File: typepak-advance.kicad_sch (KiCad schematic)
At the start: 25 parts, among them J2 Conn_01x04, J3 Conn_01x02, J5 Conn_01x32_Pin, J6 Conn_01x10, Q1 AO3407, Q2 AO3407, U1 E73-2G4M08S1C, U2 AP2112K-3.3, U3 TP4054, X1 32768kHz

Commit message: Initial Commit.
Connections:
- net P0.17: now also J5.17 (Pin_17); no longer J5.23 (Pin_23)
- net P0.22: now also J5.18 (Pin_18); no longer J5.25 (Pin_25)
- net P0.28: now also J5.23 (Pin_23); no longer J5.16 (Pin_16)
- net P1.02: now also J5.16 (Pin_16); no longer J5.17 (Pin_17)
- net P1.04: now also J5.25 (Pin_25); no longer J5.18 (Pin_18)
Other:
- note added: "LowF+A"
- moved on the sheet: R1
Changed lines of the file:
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@@
 		)
 	)
-	(text "LowF"
+	(text "LowF+A"
 		(exclude_from_sim no)
-		(at 43.18 93.472 90)
+		(at 43.18 92.202 90)
 		(effects
 			(font
@@
 		)
 	)
-	(text "LowF"
+	(text "LowF+A"
 		(exclude_from_sim no)
-		(at 48.26 93.472 90)
+		(at 48.26 92.202 90)
 		(effects
 			(font
@@
 		)
 	)
-	(text "LowF"
+	(text "LowF+A"
 		(exclude_from_sim no)
-		(at 58.42 93.472 90)
+		(at 76.2 92.202 90)
 		(effects
 			(font
@@
 	(text "LowF"
 		(exclude_from_sim no)
-		(at 60.96 93.472 90)
+		(at 58.42 93.472 90)
 		(effects
 			(font
@@
 	(text "USB Power"
 		(exclude_from_sim no)
-		(at 27.686 115.57 90)
+		(at 20.066 115.57 90)
 		(effects
 			(font
@@
 	(text "HighF"
 		(exclude_from_sim no)
-		(at 76.2 93.218 90)
+		(at 60.96 93.218 90)
 		(effects
 			(font
@@
 	(text "HighF"
 		(exclude_from_sim no)
-		(at 81.28 93.218 90)
+		(at 63.5 93.218 90)
 		(effects
 			(font
@@
 	(text "GND"
 		(exclude_from_sim no)
-		(at 20.32 112.522 90)
+		(at 27.94 112.522 90)
 		(effects
 			(font
@@
 		)
 	)
-	(text "LowF"
+	(text "LowF+A"
 		(exclude_from_sim no)
-		(at 40.64 93.472 90)
+		(at 40.64 92.202 90)
 		(effects
 			(font
@@
 		)
 	)
-	(text "LowF"
+	(text "LowF+A"
 		(exclude_from_sim no)
-		(at 63.5 93.472 90)
+		(at 81.28 92.202 90)
 		(effects
 			(font
@@
 		)
 	)
-	(text "LowF"
+	(text "LowF+A"
 		(exclude_from_sim no)
-		(at 38.1 93.472 90)
+		(at 38.1 92.202 90)
 		(effects
 			(font
@@
 	)
 	(junction
-		(at 49.53 148.59)
+		(at 27.94 148.59)
 		(diameter 0)
 		(color 0 0 0 0)
 	)
 	(junction
-		(at 43.815 148.59)
+		(at 49.53 148.59)
 		(diameter 0)
 		(color 0 0 0 0)
 	)
 	(junction
-		(at 133.35 83.82)
+		(at 27.94 139.7)
 		(diameter 0)
 		(color 0 0 0 0)
 	)
 	(junction
-		(at 133.35 91.44)
+		(at 43.815 148.59)
 		(diameter 0)
 		(color 0 0 0 0)
 	)
 	(junction
-		(at 133.35 101.6)
+		(at 133.35 83.82)
 		(diameter 0)
 		(color 0 0 0 0)
 	)
 	(junction
-		(at 214.63 142.24)
+		(at 133.35 91.44)
 		(diameter 0)
 		(color 0 0 0 0)
 	)
 	(junction
-		(at 149.86 88.9)
+		(at 133.35 101.6)
 		(diameter 0)
 		(color 0 0 0 0)
 	)
 	(junction
-		(at 27.305 139.7)
+		(at 214.63 142.24)
 		(diameter 0)
 		(color 0 0 0 0)
 	)
 	(junction
-		(at 96.52 137.795)
+		(at 149.86 88.9)
 		(diameter 0)
 		(color 0 0 0 0)
 	)
 	(junction
-		(at 27.305 148.59)
+		(at 96.52 137.795)
 		(diameter 0)
 		(color 0 0 0 0)
@@
 	(wire
 		(pts
-			(xy 27.305 161.29) (xy 27.305 162.56)
+			(xy 27.94 157.48) (xy 27.94 158.75)
 		)
 		(stroke
@@
 	(wire
 		(pts
+			(xy 27.94 139.7) (xy 36.195 139.7)
+		)
+		(stroke
+			(width 0)
+			(type default)
+		)
+	)
+	(wire
+		(pts
 			(xy 49.53 151.13) (xy 49.53 148.59)
 		)
@@
 	(wire
 		(pts
-			(xy 27.305 139.7) (xy 24.765 139.7)
+			(xy 24.765 139.7) (xy 27.94 139.7)
 		)
 		(stroke
@@
 	(wire
 		(pts
-			(xy 142.24 147.955) (xy 144.78 147.955)
+			(xy 27.94 148.59) (xy 27.94 149.86)
 		)
 		(stroke
@@
 	(wire
 		(pts
-			(xy 33.02 52.07) (xy 41.91 52.07)
+			(xy 142.24 147.955) (xy 144.78 147.955)
 		)
 		(stroke
@@
 	(wire
 		(pts
-			(xy 27.305 139.7) (xy 36.195 139.7)
+			(xy 33.02 52.07) (xy 41.91 52.07)
 		)
 		(stroke
@@
 	(wire
 		(pts
-			(xy 251.46 25.4) (xy 261.62 25.4)
+			(xy 27.94 139.7) (xy 27.94 148.59)
 		)
 		(stroke
@@
 	(wire
 		(pts
-			(xy 33.02 57.15) (xy 41.91 57.15)
+			(xy 251.46 25.4) (xy 261.62 25.4)
 		)
 		(stroke
@@
 	(wire
 		(pts
-			(xy 33.02 67.31) (xy 41.91 67.31)
+			(xy 33.02 57.15) (xy 41.91 57.15)
 		)
 		(stroke
@@
 	(wire
 		(pts
-			(xy 149.86 88.9) (xy 162.56 88.9)
+			(xy 33.02 67.31) (xy 41.91 67.31)
 		)
 		(stroke
@@
 	(wire
 		(pts
-			(xy 53.975 151.13) (xy 49.53 151.13)
+			(xy 149.86 88.9) (xy 162.56 88.9)
 		)
 		(stroke
@@
 	(wire
 		(pts
-			(xy 41.91 69.85) (xy 33.02 69.85)
+			(xy 53.975 151.13) (xy 49.53 151.13)
 		)
 		(stroke
@@
 	(wire
 		(pts
-			(xy 83.82 64.77) (xy 76.2 64.77)
+			(xy 41.91 69.85) (xy 33.02 69.85)
 		)
 		(stroke
@@
 	(wire
 		(pts
-			(xy 41.91 77.47) (xy 32.385 77.47)
+			(xy 83.82 64.77) (xy 76.2 64.77)
 		)
 		(stroke
@@
 	(wire
 		(pts
-			(xy 27.305 148.59) (xy 27.305 153.67)
+			(xy 41.91 77.47) (xy 32.385 77.47)
 		)
 		(stroke
@@
 	(wire
 		(pts
-			(xy 27.305 139.7) (xy 27.305 148.59)
-		)
-		(stroke
-			(width 0)
-			(type default)
-		)
-	)
-	(wire
-		(pts
-			(xy 27.305 148.59) (xy 31.75 148.59)
+			(xy 27.94 148.59) (xy 31.75 148.59)
 		)
 		(stroke
@@
 	(global_label "P1.04"
 		(shape input)
-		(at 63.5 104.14 90)
+		(at 81.28 104.14 90)
 		(fields_autoplaced yes)
 		(effects
@@
 		)
 		(property "Intersheetrefs" "${INTERSHEET_REFS}"
-			(at 63.5 95.6515 90)
+			(at 81.28 95.6515 90)
 			(effects
 				(font
@@
 	(global_label "P0.28"
 		(shape input)
-		(at 58.42 104.14 90)
+		(at 76.2 104.14 90)
 		(fields_autoplaced yes)
 		(effects
@@
 		)
 		(property "Intersheetrefs" "${INTERSHEET_REFS}"
-			(at 58.42 95.6515 90)
+			(at 76.2 95.6515 90)
 			(effects
 				(font
@@
 	(global_label "P0.22"
 		(shape input)
-		(at 81.28 104.14 90)
+		(at 63.5 104.14 90)
 		(fields_autoplaced yes)
 		(effects
@@
 		)
 		(property "Intersheetrefs" "${INTERSHEET_REFS}"
-			(at 81.28 95.6515 90)
+			(at 63.5 95.6515 90)
 			(effects
 				(font
@@
 	(global_label "P1.02"
 		(shape input)
-		(at 60.96 104.14 90)
+		(at 58.42 104.14 90)
 		(fields_autoplaced yes)
 		(effects
@@
 		)
 		(property "Intersheetrefs" "${INTERSHEET_REFS}"
-			(at 60.96 95.6515 90)
+			(at 58.42 95.6515 90)
 			(effects
 				(font
@@
 	(global_label "P0.17"
 		(shape input)
-		(at 76.2 104.14 90)
+		(at 60.96 104.14 90)
 		(fields_autoplaced yes)
 		(effects
@@
 		)
 		(property "Intersheetrefs" "${INTERSHEET_REFS}"
-			(at 76.2 95.6515 90)
+			(at 60.96 95.6515 90)
 			(effects
 				(font
@@
 	(symbol
 		(lib_id "nrfmicro-rescue:R")
-		(at 27.305 157.48 0)
+		(at 27.94 153.67 0)
 		(unit 1)
 		(exclude_from_sim no)
@@
 		(dnp no)
 		(property "Reference" "R1"
-			(at 29.083 156.3116 0)
+			(at 29.718 152.5016 0)
 			(effects
 				(font
@@
 		)
 		(property "Value" "100K"
-			(at 29.083 158.623 0)
+			(at 29.718 154.813 0)
 			(effects
 				(font
@@
 		)
 		(property "Footprint" "Resistor_SMD:R_0805_2012Metric_Pad1.20x1.40mm_HandSolder"
-			(at 25.527 157.48 90)
+			(at 26.162 153.67 90)
 			(effects
 				(font
@@
 		)
 		(property "Datasheet" ""
-			(at 27.305 157.48 0)
+			(at 27.94 153.67 0)
 			(effects
 				(font
@@
 		)
 		(property "Description" ""
-			(at 27.305 157.48 0)
+			(at 27.94 153.67 0)
 			(effects
 				(font
@@
 	(symbol
 		(lib_id "nrfmicro-rescue:GND")
-		(at 27.305 162.56 0)
+		(at 27.94 158.75 0)
 		(unit 1)
 		(exclude_from_sim no)
@@
 		(dnp no)
 		(property "Reference" "#PWR017"
-			(at 27.305 168.91 0)
+			(at 27.94 165.1 0)
 			(effects
 				(font
@@
 		)
 		(property "Value" "GND"
-			(at 27.305 166.37 0)
+			(at 27.94 162.56 0)
 			(effects
 				(font
@@
 		)
 		(property "Footprint" ""
-			(at 27.305 162.56 0)
+			(at 27.94 158.75 0)
 			(effects
 				(font
@@
 		)
 		(property "Datasheet" ""
-			(at 27.305 162.56 0)
+			(at 27.94 158.75 0)
 			(effects
 				(font
@@
 		)
 		(property "Description" ""
-			(at 27.305 162.56 0)
+			(at 27.94 158.75 0)
 			(effects
 				(font

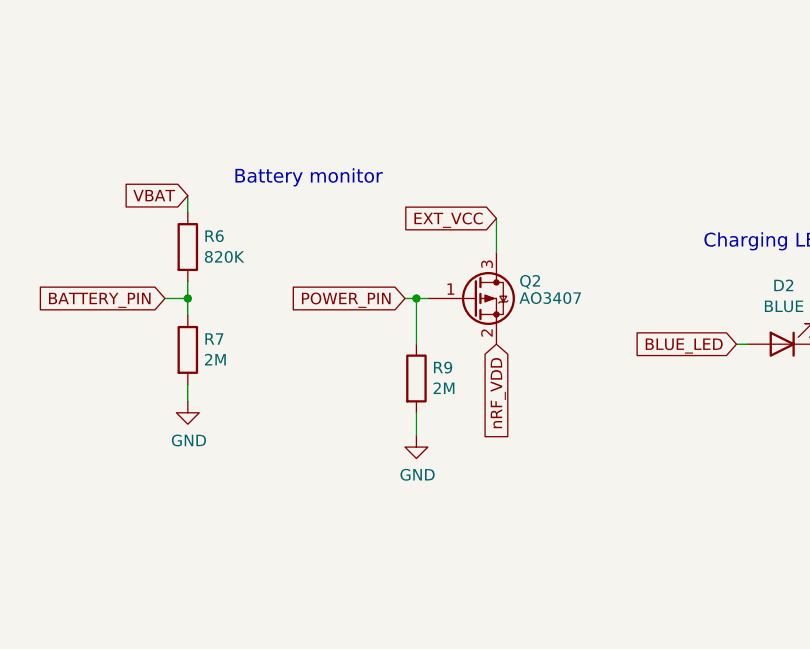
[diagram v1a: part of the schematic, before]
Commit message: Updated to hand-solder footprints.
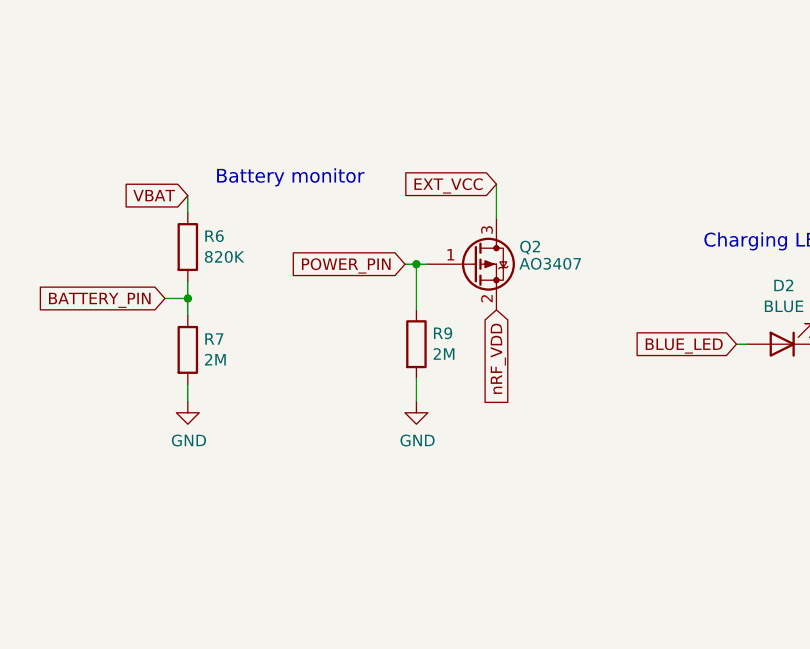
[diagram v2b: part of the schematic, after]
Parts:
- Q1, Q2: footprint Package_TO_SOT_SMD:SOT-23 -> Package_TO_SOT_SMD:SOT-23_Handsoldering
- U2, U3: footprint Package_TO_SOT_SMD:SOT-23-5 -> Package_TO_SOT_SMD:SOT-23-5_HandSoldering
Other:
- moved on the sheet: Q2, R9
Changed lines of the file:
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@@
 	(text "Battery monitor"
 		(exclude_from_sim no)
-		(at 194.31 129.794 0)
+		(at 192.278 129.794 0)
 		(effects
 			(font
@@
 	)
 	(junction
-		(at 214.63 142.24)
+		(at 214.63 138.43)
 		(diameter 0)
 		(color 0 0 0 0)
@@
 	(wire
 		(pts
-			(xy 223.52 133.35) (xy 223.52 137.16)
+			(xy 223.52 129.54) (xy 223.52 133.35)
 		)
 		(stroke
@@
 	(wire
 		(pts
-			(xy 213.36 142.24) (xy 214.63 142.24)
+			(xy 213.36 138.43) (xy 214.63 138.43)
 		)
 		(stroke
@@
 	(wire
 		(pts
-			(xy 214.63 154.94) (xy 214.63 157.48)
+			(xy 214.63 151.13) (xy 214.63 153.67)
 		)
 		(stroke
@@
 	(wire
 		(pts
-			(xy 214.63 142.24) (xy 214.63 147.32)
+			(xy 214.63 138.43) (xy 214.63 143.51)
 		)
 		(stroke
@@
 	(wire
 		(pts
-			(xy 214.63 142.24) (xy 215.9 142.24)
+			(xy 214.63 138.43) (xy 215.9 138.43)
 		)
 		(stroke
@@
 	(global_label "EXT_VCC"
 		(shape input)
-		(at 223.52 133.35 180)
+		(at 223.52 129.54 180)
 		(fields_autoplaced yes)
 		(effects
@@
 		)
 		(property "Intersheetrefs" "${INTERSHEET_REFS}"
-			(at 212.6125 133.35 0)
+			(at 212.6125 129.54 0)
 			(effects
 				(font
@@
 	(global_label "POWER_PIN"
 		(shape input)
-		(at 213.36 142.24 180)
+		(at 213.36 138.43 180)
 		(fields_autoplaced yes)
 		(effects
@@
 		)
 		(property "Intersheetrefs" "${INTERSHEET_REFS}"
-			(at 199.731 142.24 0)
+			(at 199.731 138.43 0)
 			(effects
 				(font
@@
 	(global_label "nRF_VDD"
 		(shape input)
-		(at 223.52 147.32 270)
+		(at 223.52 143.51 270)
 		(fields_autoplaced yes)
 		(effects
@@
 		)
 		(property "Intersheetrefs" "${INTERSHEET_REFS}"
-			(at 223.52 158.409 90)
+			(at 223.52 154.599 90)
 			(effects
 				(font
@@
 			)
 		)
-		(property "Footprint" "Package_TO_SOT_SMD:SOT-23"
+		(property "Footprint" "Package_TO_SOT_SMD:SOT-23_Handsoldering"
 			(at 46.355 141.605 0)
 			(effects
@@
 	(symbol
 		(lib_id "nrfmicro-rescue:BSS83P")
-		(at 220.98 142.24 0)
+		(at 220.98 138.43 0)
 		(unit 1)
 		(exclude_from_sim no)
@@
 		(dnp no)
 		(property "Reference" "Q2"
-			(at 226.06 140.335 0)
+			(at 226.06 136.525 0)
 			(effects
 				(font
@@
 		)
 		(property "Value" "AO3407"
-			(at 226.06 142.24 0)
+			(at 226.06 138.43 0)
 			(effects
 				(font
@@
 			)
 		)
-		(property "Footprint" "Package_TO_SOT_SMD:SOT-23"
-			(at 226.06 144.145 0)
+		(property "Footprint" "Package_TO_SOT_SMD:SOT-23_Handsoldering"
+			(at 226.06 140.335 0)
 			(effects
 				(font
@@
 		)
 		(property "Datasheet" ""
-			(at 220.98 142.24 0)
+			(at 220.98 138.43 0)
 			(effects
 				(font
@@
 		)
 		(property "Description" ""
-			(at 220.98 142.24 0)
+			(at 220.98 138.43 0)
 			(effects
 				(font
@@
 	(symbol
 		(lib_id "Device:R")
-		(at 214.63 151.13 0)
+		(at 214.63 147.32 0)
 		(unit 1)
 		(exclude_from_sim no)
@@
 		(dnp no)
 		(property "Reference" "R9"
-			(at 216.408 149.9616 0)
+			(at 216.408 146.1516 0)
 			(effects
 				(font
@@
 		)
 		(property "Value" "2M"
-			(at 216.408 152.273 0)
+			(at 216.408 148.463 0)
 			(effects
 				(font
@@
 		)
 		(property "Footprint" "Resistor_SMD:R_0805_2012Metric_Pad1.20x1.40mm_HandSolder"
-			(at 212.852 151.13 90)
+			(at 212.852 147.32 90)
 			(effects
 				(font
@@
 		)
 		(property "Datasheet" "~"
-			(at 214.63 151.13 0)
+			(at 214.63 147.32 0)
 			(effects
 				(font
@@
 		)
 		(property "Description" ""
-			(at 214.63 151.13 0)
+			(at 214.63 147.32 0)
 			(effects
 				(font
@@
 			)
 		)
-		(property "Footprint" "Package_TO_SOT_SMD:SOT-23-5"
+		(property "Footprint" "Package_TO_SOT_SMD:SOT-23-5_HandSoldering"
 			(at 123.19 151.765 0)
 			(effects
@@
 			)
 		)
-		(property "Footprint" "Package_TO_SOT_SMD:SOT-23-5"
+		(property "Footprint" "Package_TO_SOT_SMD:SOT-23-5_HandSoldering"
 			(at 61.595 142.875 0)
 			(effects
@@
 	(symbol
 		(lib_id "nrfmicro-rescue:GND")
-		(at 214.63 157.48 0)
+		(at 214.63 153.67 0)
 		(unit 1)
 		(exclude_from_sim no)
@@
 		(dnp no)
 		(property "Reference" "#PWR0118"
-			(at 214.63 163.83 0)
+			(at 214.63 160.02 0)
 			(effects
 				(font
@@
 		)
 		(property "Value" "GND"
-			(at 214.757 161.8742 0)
+			(at 214.757 158.0642 0)
 			(effects
 				(font
@@
 		)
 		(property "Footprint" ""
-			(at 214.63 157.48 0)
+			(at 214.63 153.67 0)
 			(effects
 				(font
@@
 		)
 		(property "Datasheet" ""
-			(at 214.63 157.48 0)
+			(at 214.63 153.67 0)
 			(effects
 				(font
@@
 		)
 		(property "Description" ""
-			(at 214.63 157.48 0)
+			(at 214.63 153.67 0)
 			(effects
 				(font
